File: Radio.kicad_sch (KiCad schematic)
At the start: 0 parts

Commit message: radio starting
Radio start + changes to the root name
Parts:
- added U2: CC2500, Package_DFN_QFN:Texas_RGP0020H_VQFN-20-1EP_4x4mm_P0.5mm_EP2.4x2.4mm, symbol RF:CC2500
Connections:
- new net: U2.11 (AVDD), U2.14 (AVDD), U2.15 (AVDD), U2.9 (AVDD)
- new net: U2.16 (GND), U2.19 (GND), U2.21 (GND)
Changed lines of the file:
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@@
 	(generator_version "10.0")
 	(paper "A4")
+	(symbol
+		(lib_id "RF:CC2500")
+		(at 81.28 71.12 0)
+		(unit 1)
+		(body_style 1)
+		(exclude_from_sim no)
+		(in_bom yes)
+		(on_board yes)
+		(in_pos_files yes)
+		(dnp no)
+		(fields_autoplaced yes)
+		(property "Reference" "U2"
+			(at 83.4233 86.36 0)
+			(show_name no)
+			(do_not_autoplace no)
+			(effects
+				(font
+					(size 1.27 1.27)
+				)
+				(justify left)
+			)
+		)
+		(property "Value" "CC2500"
+			(at 83.4233 88.9 0)
+			(show_name no)
+			(do_not_autoplace no)
+			(effects
+				(font
+					(size 1.27 1.27)
+				)
+				(justify left)
+			)
+		)
+		(property "Footprint" "Package_DFN_QFN:Texas_RGP0020H_VQFN-20-1EP_4x4mm_P0.5mm_EP2.4x2.4mm"
+			(at 82.55 88.9 0)
+			(hide yes)
+			(show_name no)
+			(do_not_autoplace no)
+			(effects
+				(font
+					(size 1.27 1.27)
+				)
+			)
+		)
+		(property "Datasheet" "http://www.ti.com/lit/ds/symlink/cc2500.pdf"
+			(at 86.36 55.88 0)
+			(hide yes)
+			(show_name no)
+			(do_not_autoplace no)
+			(effects
+				(font
+					(size 1.27 1.27)
+				)
+			)
+		)
+		(property "Description" "Single Chip Low Power RF Transceiver, QFN-20"
+			(at 81.28 71.12 0)
+			(hide yes)
+			(show_name no)
+			(do_not_autoplace no)
+			(effects
+				(font
+					(size 1.27 1.27)
+				)
+			)
+		)
+		(pin "1"
+		)
+		(pin "6"
+		)
+		(pin "7"
+		)
+		(pin "3"
+		)
+		(pin "4"
+		)
+		(pin "5"
+		)
+		(pin "8"
+		)
+		(pin "2"
+		)
+		(pin "10"
+		)
+		(pin "18"
+		)
+		(pin "19"
+		)
+		(pin "13"
+		)
+		(pin "20"
+		)
+		(pin "21"
+		)
+		(pin "16"
+		)
+		(pin "14"
+		)
+		(pin "9"
+		)
+		(pin "15"
+		)
+		(pin "17"
+		)
+		(pin "11"
+		)
+		(pin "12"
+		)
+		(instances
+			(project "Drone_FC_project"
+				(path "/b2b6b395-2e98-42cf-8acc-86126f9affef/de504034-d36e-4db9-a65e-8e2d9c74c2b5"
+					(reference "U2")
+					(unit 1)
+				)
+			)
+		)
+	)
 )

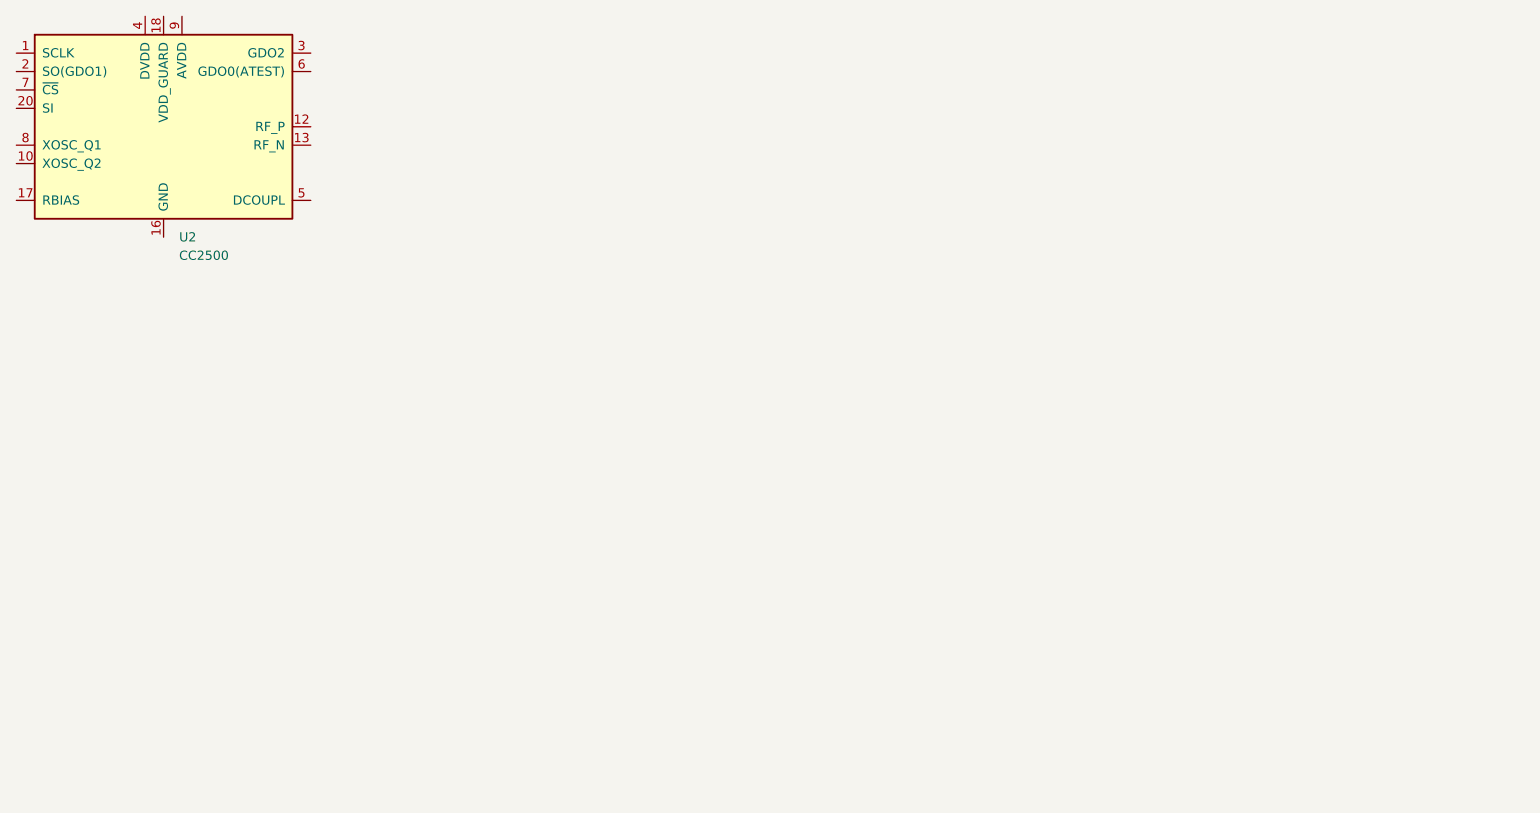
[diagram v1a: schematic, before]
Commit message: Created radio, cleanup a few other things
Finished radio schematic, added datasheets, added a stm32cubemx file for pinouts, added SPI1 and SPI2.
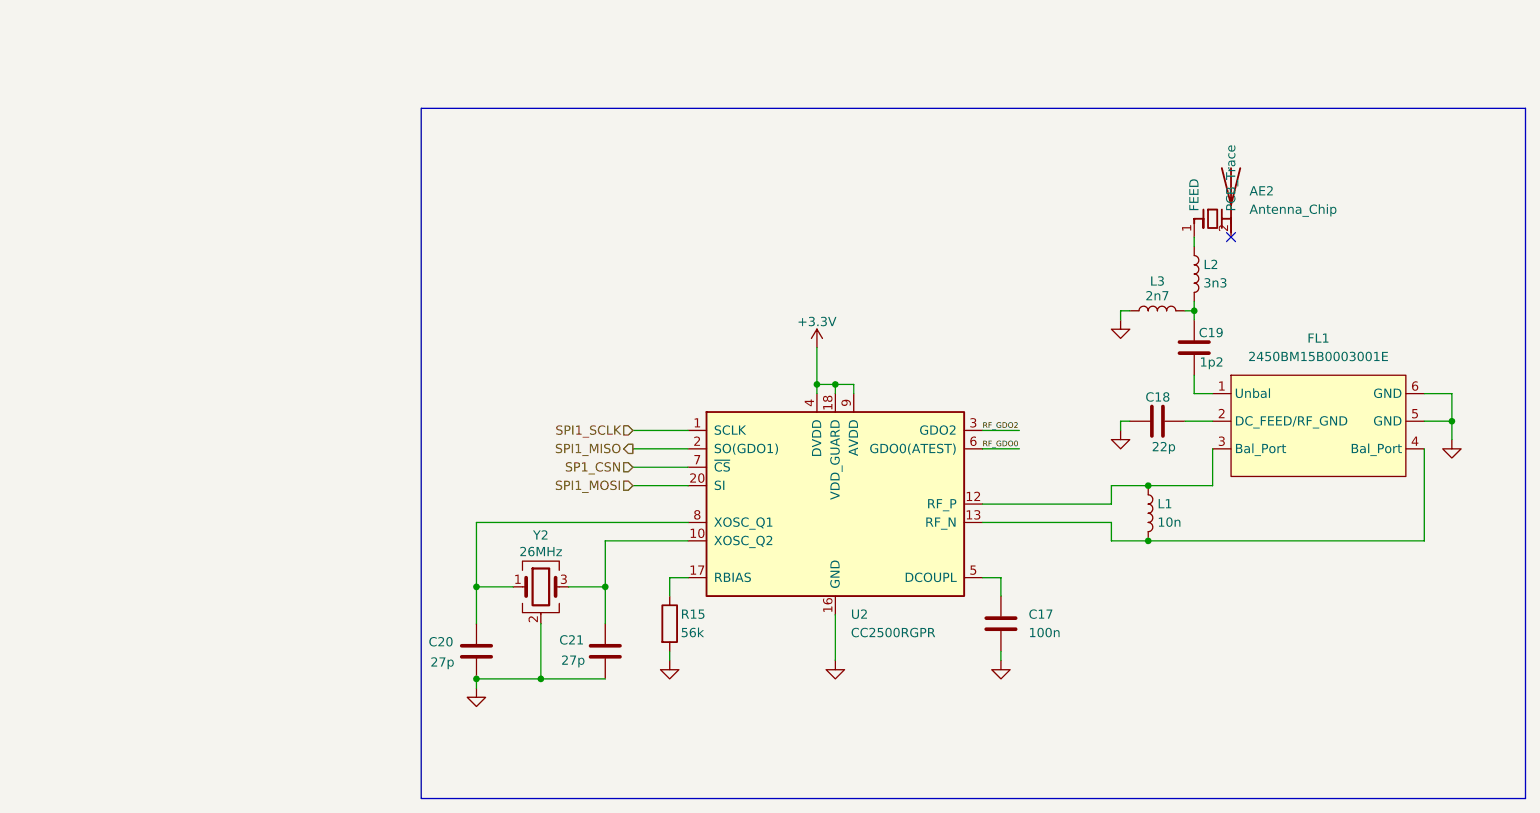
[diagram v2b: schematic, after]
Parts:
- added AE2: Antenna_Chip, Package_DFN_QFN:DFN-8-1EP_2x3mm_P0.5mm_EP0.61x2.2mm, symbol Device:Antenna_Chip
- added C17: 100n, symbol Device:C
- added C18: 22p, symbol Device:C
- added C19: 1p2, symbol Device:C
- added C20, C21: 27p, Capacitor_SMD:C_0603_1608Metric, symbol Device:C
- added FL1: 2450BM15B0003001E, RF_Converter:Balun_Johanson_0896BM15A0001, symbol Drone_custom_symbols:2450BM15B0003001E
- added L1: 10n, Package_SO:SOIC-20W_7.5x12.8mm_P1.27mm, symbol Device:L
- added L2: 3n3, Package_SO:SOIC-20W_7.5x12.8mm_P1.27mm, symbol Device:L
- added L3: 2n7, Package_SO:SOIC-20W_7.5x12.8mm_P1.27mm, symbol Device:L
- added R15: 56k, symbol Device:R
- added Y2: 26MHz, symbol Device:Crystal_GND24
- U2: value CC2500 -> CC2500RGPR
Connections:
- net SPI1_SCLK: now reaches U2.1 (SCLK)
- net at U2.10 (XOSC_Q2): now also C21.1, Y2.3
- net +3.3V: now reaches U2.11 (AVDD), U2.14 (AVDD), U2.15 (AVDD), U2.9 (AVDD)
- net +3.3V: now also U2.18 (VDD_GUARD), U2.4 (DVDD)
- net at U2.12 (RF_P): now also FL1.3 (Bal_Port), L1.1
- net at U2.13 (RF_N): now also FL1.4 (Bal_Port), L1.2
- net GND: now reaches U2.16 (GND), U2.19 (GND), U2.21 (GND)
- net GND: now also C17.2, C18.1, C20.2, C21.2, FL1.5 (GND), FL1.6 (GND), L3.1, R15.2, Y2.2 (G), Y2.4 (G)
- net at U2.17 (RBIAS): now also R15.1
- net SPI1_MISO: now reaches U2.2 (SO(GDO1))
- net SPI1_MOSI: now reaches U2.20 (SI)
- net RF_GDO2: now reaches U2.3 (GDO2)
- net at U2.5 (DCOUPL): now also C17.1
- net RF_GDO0: now reaches U2.6 (GDO0(ATEST))
- net SP1_CSN: now reaches U2.7 (~{CS})
- net at U2.8 (XOSC_Q1): now also C20.1, Y2.1
- new net: C18.2, FL1.2 (DC_FEED/RF_GND)
- new net: C19.1, FL1.1 (Unbal)
- new net: AE2.1 (FEED), L2.1
- new net: C19.2, L2.2, L3.2
- no-connect marks 0 -> 1
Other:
- moved on the sheet: U2

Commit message: Fixing some radio things
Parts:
- AE2: value Antenna_Chip -> 2450AT18B100E
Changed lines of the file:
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@@
 	(wire
 		(pts
-			(xy 194.31 113.03) (xy 199.39 113.03)
+			(xy 194.31 113.03) (xy 200.66 113.03)
 		)
 		(stroke
@@
 	(wire
 		(pts
-			(xy 194.31 115.57) (xy 199.39 115.57)
+			(xy 194.31 115.57) (xy 200.66 115.57)
 		)
 		(stroke
@@
 		)
 	)
+	(hierarchical_label "RF_GDO0"
+		(shape output)
+		(at 200.66 115.57 0)
+		(effects
+			(font
+				(size 1.27 1.27)
+			)
+			(justify left)
+		)
+	)
 	(hierarchical_label "SP1_CSN"
 		(shape input)
@@
 			)
 			(justify right)
+		)
+	)
+	(hierarchical_label "RF_GDO2"
+		(shape output)
+		(at 200.66 113.03 0)
+		(effects
+			(font
+				(size 1.27 1.27)
+			)
+			(justify left)
 		)
 	)
@@
 			)
 		)
-		(property "Value" "Antenna_Chip"
+		(property "Value" "2450AT18B100E"
 			(at 231.14 82.5499 0)
 			(show_name no)

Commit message: footprints and spacing
Added half the footprints and made thigns look nicer.
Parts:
- AE2: footprint Package_DFN_QFN:DFN-8-1EP_2x3mm_P0.5mm_EP0.61x2.2mm -> RF_Antenna:XDCR_2450AT18B100E
- C17, C18, C19: footprint (none) -> Capacitor_SMD:C_0402_1005Metric
- C20, C21: footprint Capacitor_SMD:C_0603_1608Metric -> Capacitor_SMD:C_0402_1005Metric
- L1, L2, L3: footprint Package_SO:SOIC-20W_7.5x12.8mm_P1.27mm -> Inductor_SMD:L_0402_1005Metric
- R15: footprint (none) -> Resistor_SMD:R_0402_1005Metric
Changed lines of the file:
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@@
 			)
 		)
-		(property "Footprint" ""
+		(property "Footprint" "Capacitor_SMD:C_0402_1005Metric"
 			(at 222.25 110.7948 0)
 			(hide yes)
@@
 			)
 		)
-		(property "Footprint" "Capacitor_SMD:C_0603_1608Metric"
+		(property "Footprint" "Capacitor_SMD:C_0402_1005Metric"
 			(at 125.4252 147.32 0)
 			(hide yes)
@@
 			)
 		)
-		(property "Footprint" "Package_SO:SOIC-20W_7.5x12.8mm_P1.27mm"
+		(property "Footprint" "Inductor_SMD:L_0402_1005Metric"
 			(at 223.52 91.44 0)
 			(hide yes)
@@
 			)
 		)
-		(property "Footprint" "Package_SO:SOIC-20W_7.5x12.8mm_P1.27mm"
+		(property "Footprint" "Inductor_SMD:L_0402_1005Metric"
 			(at 217.17 124.46 0)
 			(hide yes)
@@
 			)
 		)
-		(property "Footprint" ""
+		(property "Footprint" "Capacitor_SMD:C_0402_1005Metric"
 			(at 222.5548 97.79 0)
 			(hide yes)
@@
 			)
 		)
-		(property "Footprint" ""
+		(property "Footprint" "Capacitor_SMD:C_0402_1005Metric"
 			(at 197.8152 143.51 0)
 			(hide yes)
@@
 			)
 		)
-		(property "Footprint" "Package_DFN_QFN:DFN-8-1EP_2x3mm_P0.5mm_EP0.61x2.2mm"
+		(property "Footprint" "RF_Antenna:XDCR_2450AT18B100E"
 			(at 223.52 79.375 0)
 			(hide yes)
@@
 			)
 		)
-		(property "Footprint" "Capacitor_SMD:C_0603_1608Metric"
+		(property "Footprint" "Capacitor_SMD:C_0402_1005Metric"
 			(at 143.2052 147.32 0)
 			(hide yes)
@@
 			)
 		)
-		(property "Footprint" "Package_SO:SOIC-20W_7.5x12.8mm_P1.27mm"
+		(property "Footprint" "Inductor_SMD:L_0402_1005Metric"
 			(at 218.44 96.52 0)
 			(hide yes)
@@
 			)
 		)
-		(property "Footprint" ""
+		(property "Footprint" "Resistor_SMD:R_0402_1005Metric"
 			(at 149.352 139.7 90)
 			(hide yes)

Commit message: more footprint work and downloaded some
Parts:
- U2: footprint Package_DFN_QFN:Texas_RGP0020H_VQFN-20-1EP_4x4mm_P0.5mm_EP2.4x2.4mm -> drone_libary:QFN-20_CC2500RGPR
- Y2: footprint (none) -> drone_libary:Crystal_SMD_3225-4P(16_26MHz)
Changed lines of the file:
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@@
 			)
 		)
-		(property "Footprint" "Package_DFN_QFN:Texas_RGP0020H_VQFN-20-1EP_4x4mm_P0.5mm_EP2.4x2.4mm"
+		(property "Footprint" "drone_libary:QFN-20_CC2500RGPR"
 			(at 175.26 140.97 0)
 			(hide yes)
@@
 			)
 		)
-		(property "Footprint" ""
+		(property "Footprint" "drone_libary:Crystal_SMD_3225-4P(16_26MHz)"
 			(at 133.35 134.62 0)
 			(hide yes)
